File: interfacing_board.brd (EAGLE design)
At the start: 85.1 x 74.6 mm, 46 parts, among them IC1 MAX3096CSE, X1 87758-3816, X2 87758-3816

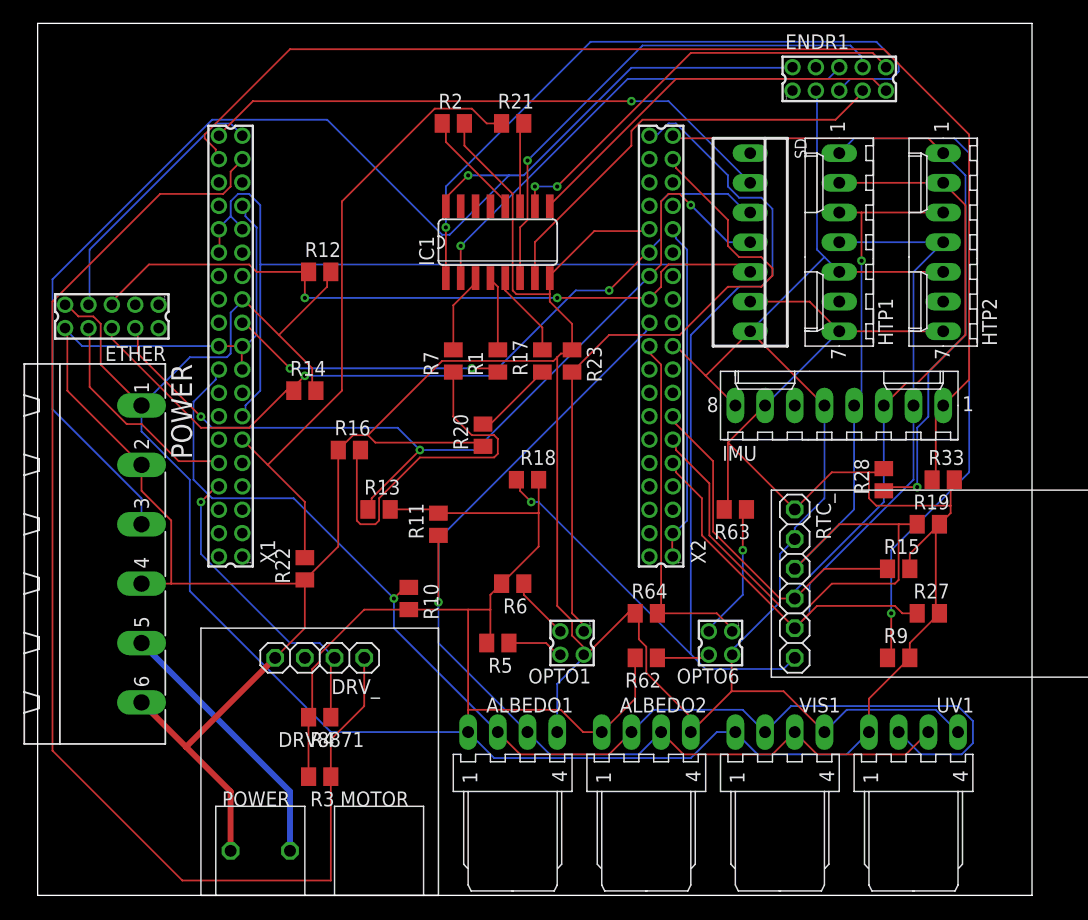
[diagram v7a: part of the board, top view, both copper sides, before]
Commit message: Schematics reorganised to be more readable.
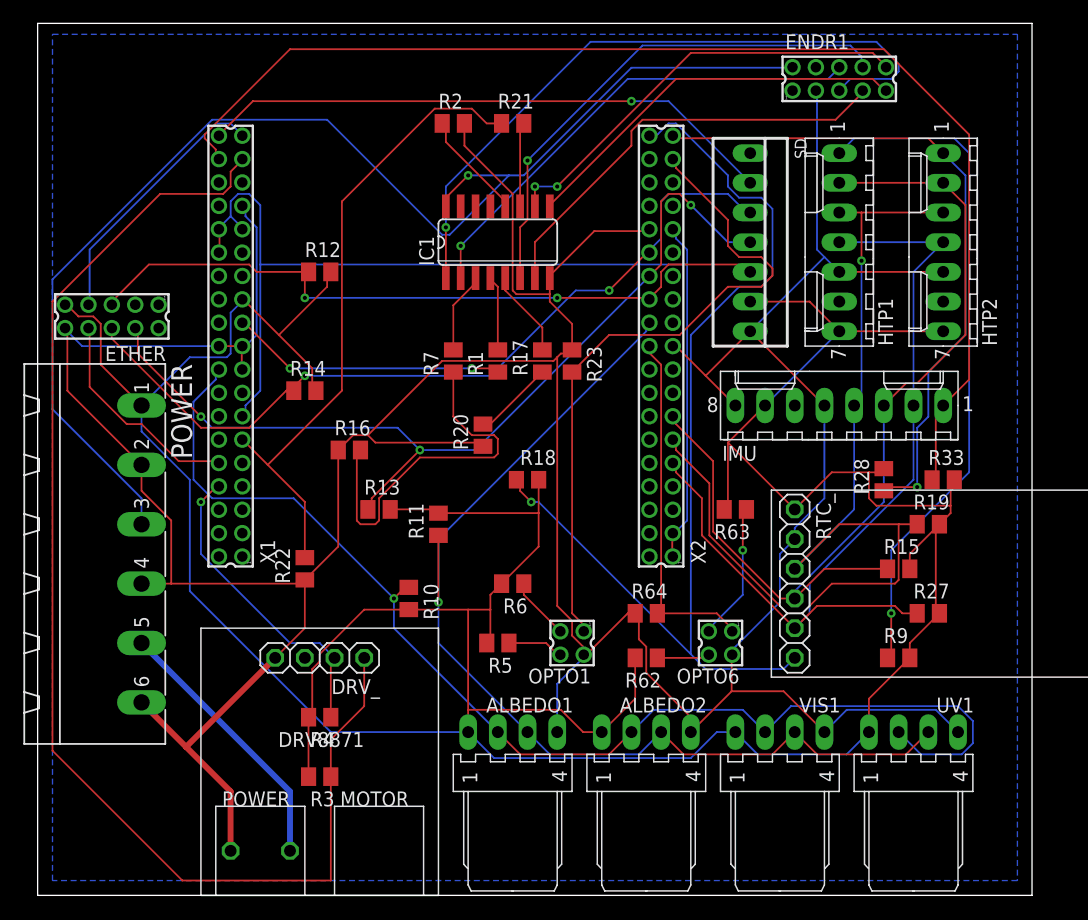
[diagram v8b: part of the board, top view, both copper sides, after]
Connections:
- net CHA-2L renamed PA1
- net CHB-2L renamed PB10
- net CHC-2L renamed PB11
- net M21 renamed PA2
- net M22 renamed PA3
- net OL_RX renamed PA9
- net OL_TX renamed PA10
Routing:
- added copper zone on layer 16, net GND
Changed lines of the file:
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@@
 <via x="22.86" y="73.9775" extent="1-16" drill="0.35"/>
 </signal>
-<signal name="OL_RX">
+<signal name="PA9">
 <contactref element="X2" pad="18"/>
 </signal>
@@
 <contactref element="X2" pad="8"/>
 </signal>
-<signal name="OL_TX">
+<signal name="PA10">
 <contactref element="X2" pad="6"/>
 </signal>
@@
 <wire x1="44.45" y1="68.8975" x2="44.45" y2="47.625" width="0.1524" layer="1"/>
 <wire x1="46.6725" y1="43.4975" x2="46.72" y2="43.45" width="0.1524" layer="1"/>
+<polygon width="0.1524" layer="16" isolate="0.6096">
+<vertex x="1.27" y="96.52"/>
+<vertex x="83.82" y="96.52"/>
+<vertex x="83.82" y="24.13"/>
+<vertex x="1.27" y="24.13"/>
+</polygon>
 </signal>
 <signal name="PA15">
@@
 <wire x1="25.0825" y1="33.02" x2="25.08" y2="33.02" width="0.1524" layer="1"/>
 </signal>
-<signal name="M22">
+<signal name="PA3">
 <contactref element="X2" pad="2"/>
 </signal>
-<signal name="M21">
+<signal name="PA2">
 <contactref element="X2" pad="4"/>
 </signal>
@@
 <wire x1="19.685" y1="59.69" x2="26.035" y2="66.04" width="0.1524" layer="1"/>
 </signal>
-<signal name="CHA-2L">
+<signal name="PA1">
 <contactref element="X1" pad="9"/>
 </signal>
-<signal name="CHB-2L">
+<signal name="PB10">
 <contactref element="X2" pad="14"/>
 </signal>
-<signal name="CHC-2L">
+<signal name="PB11">
 <contactref element="X2" pad="21"/>
 </signal>
